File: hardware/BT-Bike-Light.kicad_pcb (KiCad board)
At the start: 4 copper layers, 35 x 80 mm, 40 parts, among them J101 USB_C_Charge_Port, J102 Conn_ARM_SWD_TagConnect_TC203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, J103 BATT, Q101 DMN3731U-7, SW102 Button, U101 BT840, U102 nPM1300, U103 FEM11-F09, U105 TPS92201

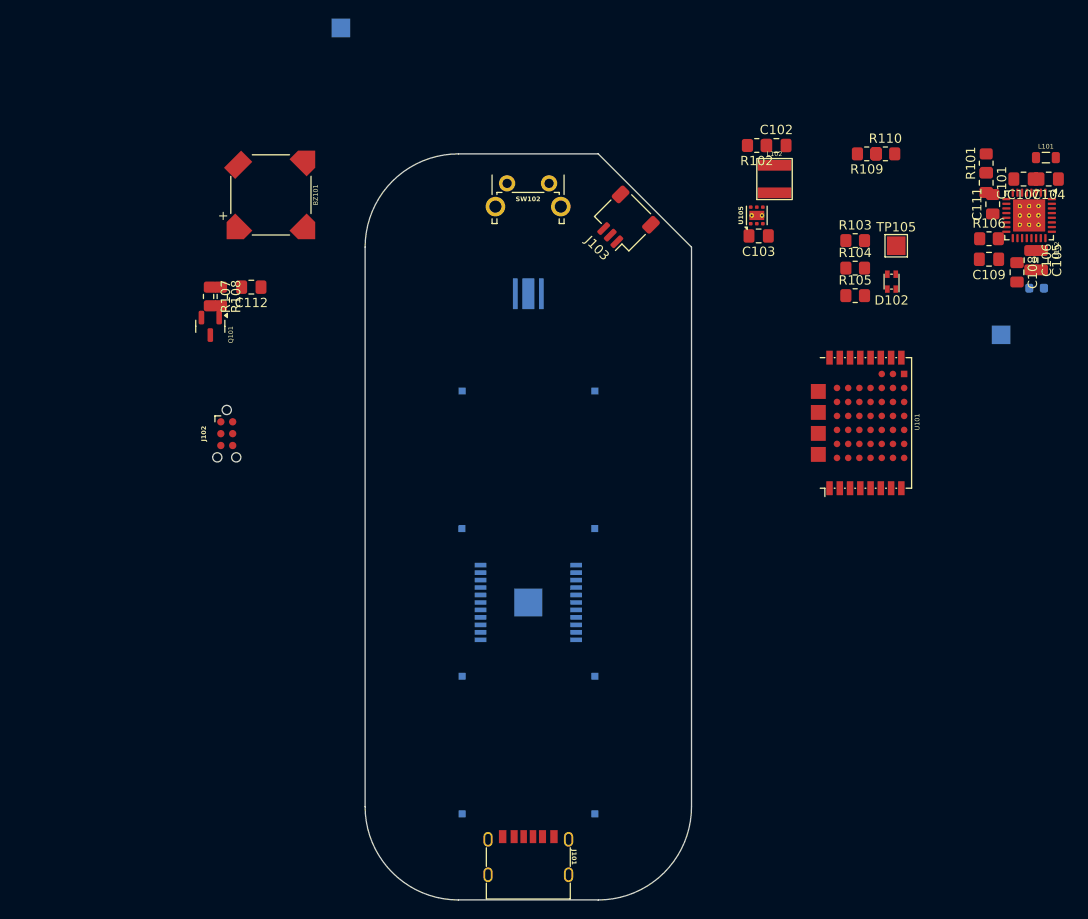
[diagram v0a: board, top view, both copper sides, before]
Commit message: Battery management IC component placement
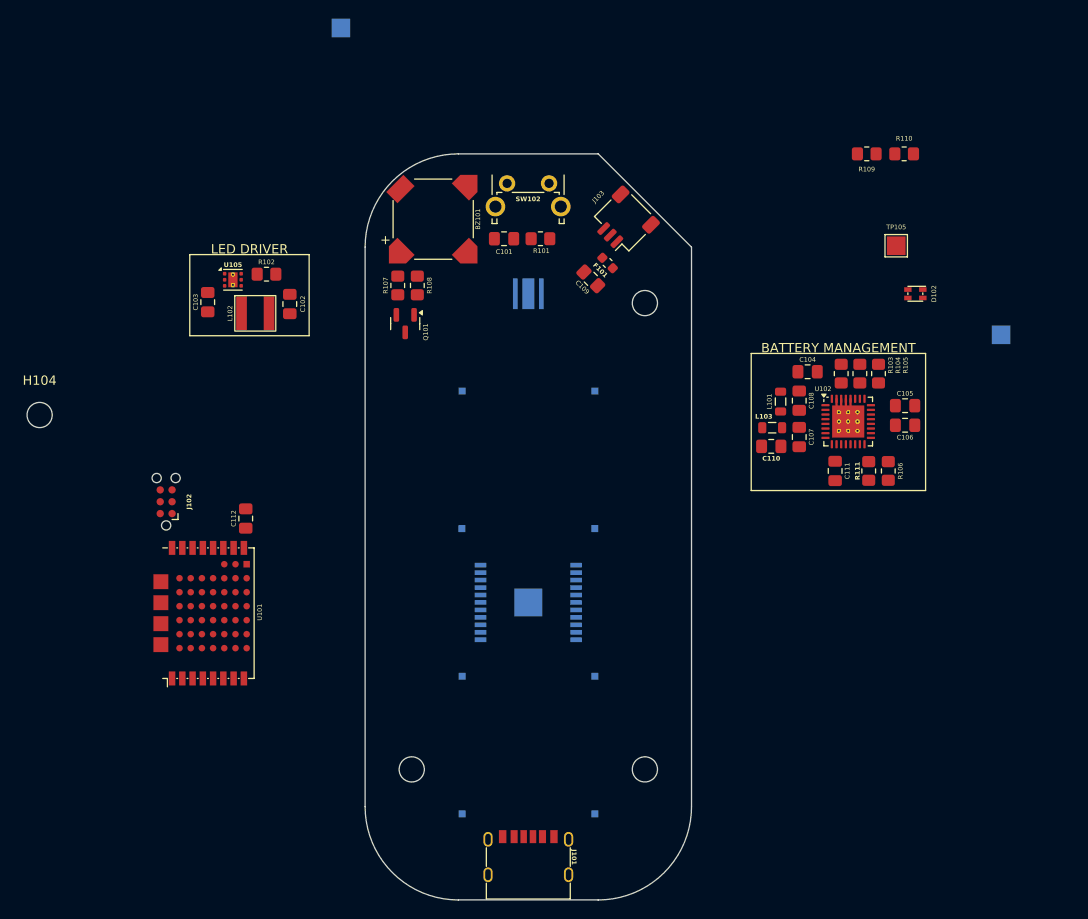
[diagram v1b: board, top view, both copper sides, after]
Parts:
- added C110: 10uF, Capacitor_SMD:C_0805_2012Metric_Pad1.18x1.45mm_HandSolder, F.Cu at (168.6, 96.4)
- added H101: M2.5, MountingHole:MountingHole_2.7mm_M2.5, F.Cu at (130.0, 131.0)
- added H102: M2.5, MountingHole:MountingHole_2.7mm_M2.5, F.Cu at (155.0, 131.0)
- added H103: M2.5, MountingHole:MountingHole_2.7mm_M2.5, F.Cu at (155.0, 81.0)
- added H104: M2.5, MountingHole:MountingHole_2.7mm_M2.5, F.Cu at (90.1, 93.0)
- added L103: 2.2uH, Inductor_SMD:L_0805_2012Metric, F.Cu at (168.7, 94.4)
- added R111: 68k, Resistor_SMD:R_0805_2012Metric_Pad1.20x1.40mm_HandSolder, F.Cu at (179.0, 99.0)
- F101: moved to F.Cu
- moved U101 73.4 mm to (104.3, 121.2)
- moved C103 59.5 mm to (108.1, 80.9), turned to -90 degrees
- moved L102 57.5 mm to (113.2, 82.1), turned to 0 degrees
- moved U105 56.6 mm to (110.8, 78.5), turned to 0 degrees
- moved C102 54.9 mm to (116.9, 81.1), turned to 90 degrees
- moved R102 54.4 mm to (114.4, 77.9)
- moved C101 52.0 mm to (139.9, 74.1), turned to 180 degrees
- moved R101 48.5 mm to (143.8, 74.1), turned to 0 degrees
- moved F101 46.1 mm to (151.0, 76.7), turned to -45 degrees
- moved C109 42.8 mm to (149.2, 78.4), turned to 135 degrees
- moved L101 38.7 mm to (169.6, 91.6), turned to 90 degrees
- moved C107 36.7 mm to (171.6, 95.4), turned to -90 degrees
- moved C111 33.2 mm to (175.4, 99.0), turned to -90 degrees
- moved C104 33.1 mm to (172.4, 88.4), turned to 0 degrees
- moved U102 29.4 mm to (176.8, 93.7), turned to 0 degrees
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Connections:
- U102 pad 16: GND -> Net-(U102-VSET2)
- U102 pad 32: unconnected-(U102-VOUT2-Pad32) -> +2V6
- U102 pad 5: unconnected-(U102-SW2-Pad5) -> Net-(U102-SW2)
- U102 pad 6: unconnected-(U102-PVSS2-Pad6) -> GND
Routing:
- net GND: track 0.00 -> 6.16 mm
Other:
- board text added: "BATTERY MANAGEMENT"
- board text added: "LED DRIVER"
- board text removed: "+"
- board text removed: "-"

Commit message: Component placement
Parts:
- removed H104: M2.5, MountingHole:MountingHole_2.7mm_M2.5
- TP105: value 1V8 -> 2V6; moved to B.Cu
- moved D102 69.8 mm to (149.1, 140.4), turned to 0 degrees
- moved TP103 65.7 mm to (127.7, 80.0), turned to 180 degrees
- moved TP105 63.4 mm to (130.2, 111.5), turned to 180 degrees
- moved R110 59.1 mm to (142.2, 107.9), turned to -90 degrees
- moved R109 57.7 mm to (140.2, 107.9), turned to -90 degrees
- moved BZ101 46.0 mm to (131.0, 118.0), turned to 180 degrees
- moved TP104 41.3 mm to (143.5, 87.0), turned to 0 degrees
- moved C105 35.1 mm to (149.0, 83.0), turned to 180 degrees
- moved U101 33.4 mm to (132.9, 104.1)
- moved R105 33.3 mm to (147.0, 85.1), turned to 0 degrees
- moved C106 33.1 mm to (152.1, 82.2), turned to 90 degrees
- moved C112 32.4 mm to (140.1, 87.5), turned to 180 degrees
- moved R108 32.4 mm to (132.0, 111.5), turned to 180 degrees
- moved J102 31.5 mm to (131.0, 86.7), turned to 0 degrees
- moved R104 31.1 mm to (147.0, 87.1), turned to 0 degrees
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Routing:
- net VSYS: track 0.00 -> 17.7 mm, vias 0 -> 2
- net GND: track 6.16 -> 19.7 mm
- net +2V6: track 0.00 -> 12.6 mm, vias 0 -> 2
- net +1V8: track 0.00 -> 5.84 mm
- net Net-(U102-SW1): track 0.00 -> 5.72 mm
- net Net-(U102-SW2): track 0.00 -> 5.46 mm
- net Net-(U102-VSET1): track 0.00 -> 3.41 mm
- net VBUSOUT: track 0.00 -> 3.41 mm
- net Net-(U105-SW): track 0.00 -> 2.97 mm
- net VBUS: track 0.00 -> 2.81 mm
- net /LED_R: track 0.00 -> 2.50 mm
- net /LED_B: track 0.00 -> 2.50 mm
- net Net-(D101-A): track 0.00 -> 2.24 mm
- net Net-(U102-VSET2): track 0.00 -> 2.05 mm
- net Net-(D101-K): track 0.00 -> 1.73 mm
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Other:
- board text added: "BLUETOOTH"
- board text added: "BUZZER"
- board text added: "POWER MGMT"
- board text removed: "BATTERY MANAGEMENT"

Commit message: Schematic cleanup
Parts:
- moved BZ101 5.00 mm to (131.0, 113.0)
- moved C101 5.00 mm to (139.9, 69.1)
- moved C102 5.00 mm to (133.7, 66.1)
- moved C103 5.00 mm to (133.5, 74.9)
- moved C104 5.00 mm to (146.8, 87.7)
- moved C105 5.00 mm to (149.0, 78.0)
- moved C106 5.00 mm to (152.1, 77.2)
- moved C107 5.00 mm to (153.8, 88.6)
- moved C108 5.00 mm to (149.9, 88.6)
- moved C109 5.00 mm to (157.2, 70.6)
- moved C110 5.00 mm to (154.8, 91.6)
- moved C111 5.00 mm to (157.4, 84.8)
- moved C112 5.00 mm to (140.1, 82.5)
- moved D101 5.00 mm to (142.5, 75.0)
- moved D102 5.00 mm to (149.1, 135.4)
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
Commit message: Route board
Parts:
- removed R103, R104, R105: 110, Resistor_SMD:R_0805_2012Metric_Pad1.20x1.40mm_HandSolder
- added TP101: VBUS, TestPoint:TestPoint_Pad_2.0x2.0mm, B.Cu at (155.3, 133.2)
- J102: value Conn_ARM_SWD_TagConnect_TC2030-NL -> TagConnect; moved to B.Cu
- moved R109 0.30 mm to (139.9, 102.9)
- moved R110 0.30 mm to (141.9, 102.9)
- moved C101 0.15 mm to (139.8, 69.1)
- moved R101 0.15 mm to (143.7, 69.1)
- turned D102 to 180 degrees
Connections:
- D102 pad 1: Net-(D102-GK) -> /LED_G
- D102 pad 2: Net-(D102-BK) -> /LED_B
- D102 pad 4: Net-(D102-RK) -> /LED_R
- U101 pad 1: unconnected-(U101-P0.26-Pad1) -> /BUZZER
- U101 pad 11: /BUZZER -> /BTN
- U101 pad 12: unconnected-(U101-P1.00-Pad12) -> /LED_EN
- U101 pad 13: unconnected-(U101-P0.13-Pad13) -> /LED_PWM
- U101 pad 2: /LED_EN -> unconnected-(U101-P0.27-Pad2)
- U101 pad 3: /LED_PWM -> unconnected-(U101-P0.00-Pad3)
- U101 pad 6: /BTN -> unconnected-(U101-P0.03-Pad6)
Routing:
- net VSYS: track 17.7 -> 156.6 mm, vias 2 -> 4
- net VBUS: track 2.81 -> 84.4 mm, vias 0 -> 2
- net +1V8: track 5.84 -> 79.4 mm, vias 0 -> 3
- net Net-(J101-CC1): track 0.00 -> 58.7 mm
- net GND: track 19.7 -> 78.3 mm, vias 0 -> 140
- net /LED_R: track 2.50 -> 59.4 mm
- net Net-(J101-CC2): track 0.00 -> 56.5 mm
- net /LED_G: track 1.70 -> 56.9 mm
- net /LED_B: track 2.50 -> 56.3 mm
- net /BTN: track 0.00 -> 48.3 mm, vias 0 -> 2
- net +2V6: track 12.6 -> 60.4 mm, vias 2 -> 1
- net /SDA: track 0.00 -> 33.4 mm, vias 0 -> 2
- net /SCL: track 0.00 -> 33.1 mm, vias 0 -> 3
- net Net-(D101-K): track 1.73 -> 18.4 mm, vias 0 -> 1
- net /BATT_NTC: track 0.00 -> 16.1 mm, vias 0 -> 2
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- added copper zone on B.Cu, net GND
- added copper zone on F.Cu, net GND
- added copper zone on In1.Cu, net GND
- added copper zone on In2.Cu, net GND

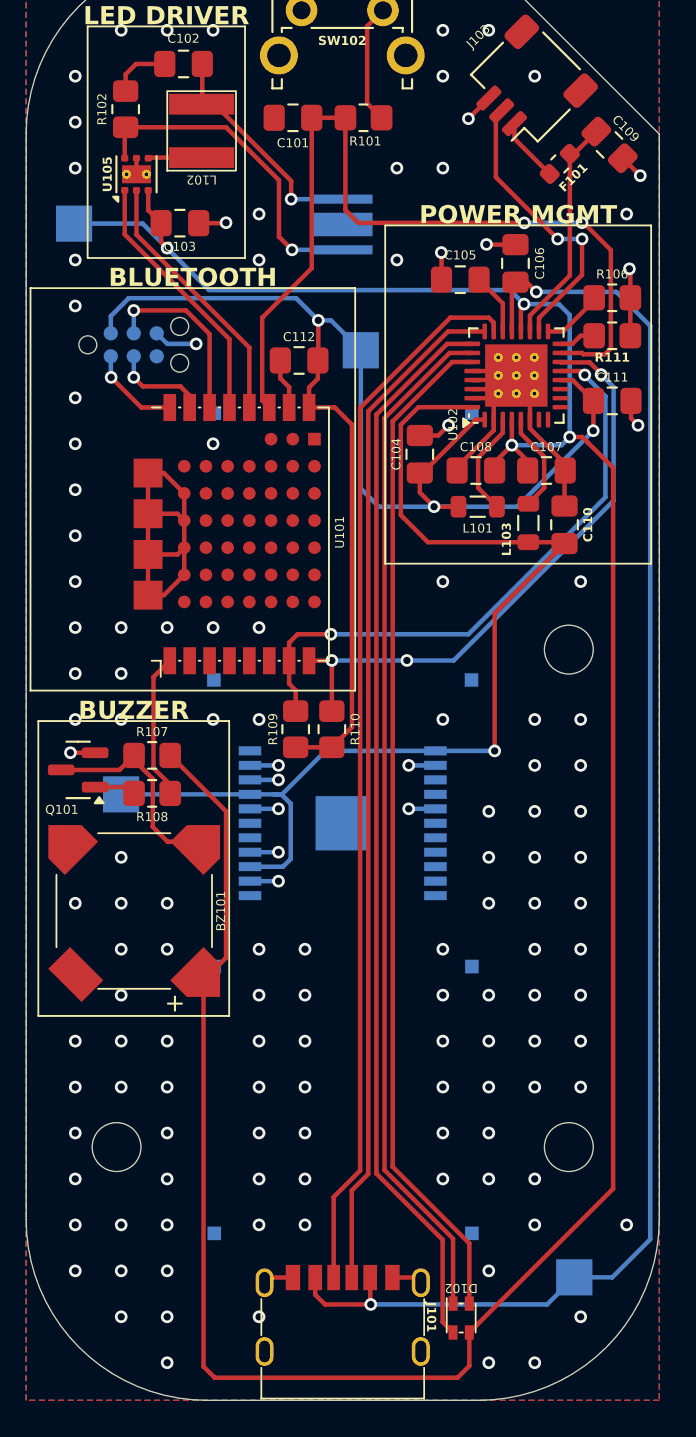
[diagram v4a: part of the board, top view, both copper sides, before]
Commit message: Combine 1V8 and 2V6 line to 2V6
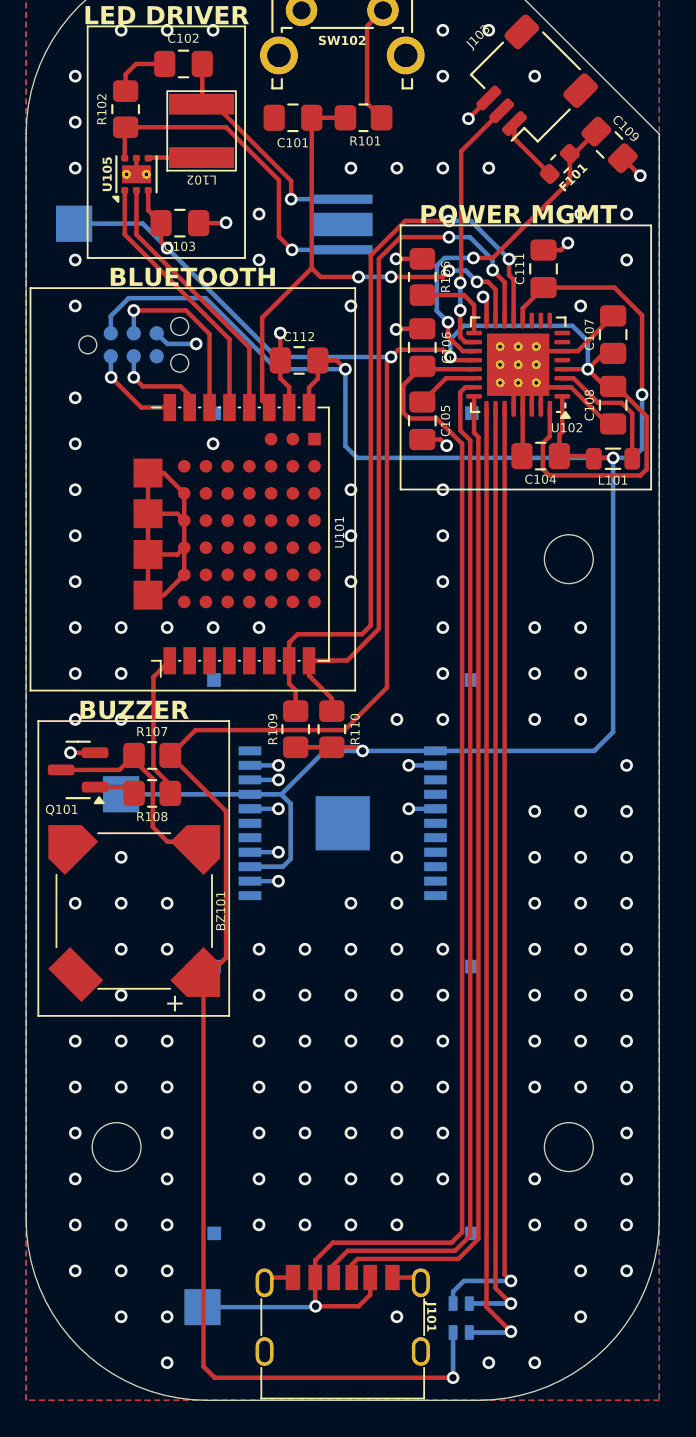
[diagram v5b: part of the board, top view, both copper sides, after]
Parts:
- removed C110: 10uF, Capacitor_SMD:C_0805_2012Metric_Pad1.18x1.45mm_HandSolder
- removed L103: 2.2uH, Inductor_SMD:L_0805_2012Metric
- removed R111: 68k, Resistor_SMD:R_0805_2012Metric_Pad1.20x1.40mm_HandSolder
- removed TP104: 1V8, TestPoint:TestPoint_Pad_2.0x2.0mm
- D102: moved to B.Cu
- R106: value 47k -> 68k
- moved TP101 20.6 mm to (134.8, 134.8)
- moved R106 10.6 mm to (146.9, 77.9), turned to -90 degrees
- moved C108 8.40 mm to (157.4, 85.0), turned to -90 degrees
- moved C107 8.37 mm to (157.4, 81.1), turned to 90 degrees
- moved C111 8.23 mm to (153.6, 77.5), turned to 90 degrees
- moved C105 8.08 mm to (146.9, 85.8), turned to -90 degrees
- moved L101 7.94 mm to (157.4, 88.0)
- moved C106 6.94 mm to (146.9, 81.8)
- moved C104 6.68 mm to (153.4, 87.8), turned to 180 degrees
- moved H103 5.00 mm to (155.0, 93.5)
- moved U102 0.61 mm to (152.2, 82.8), turned to 180 degrees
- turned D102 to 0 degrees
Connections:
- C104 pad 1: +1V8 -> +2V6
- C111 pad 1: +1V8 -> +2V6
- C112 pad 1: +1V8 -> +2V6
- J102 pad 1: +1V8 -> +2V6
- L101 pad 2: +1V8 -> +2V6
- R109 pad 2: +1V8 -> +2V6
- R110 pad 2: +1V8 -> +2V6
- U101 pad 9: +1V8 -> +2V6
- U102 pad 1: +1V8 -> +2V6
- U102 pad 12: +1V8 -> +2V6
- U102 pad 16: Net-(U102-VSET2) -> GND
- U102 pad 32: +2V6 -> VSYS
- U102 pad 5: Net-(U102-SW2) -> unconnected-(U102-SW2-Pad5)
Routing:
- net +1V8: track 79.4 -> 0.00 mm, vias 3 -> 0
- net +2V6: track 60.4 -> 117.6 mm, vias 1 -> 4
- net /BTN: track 48.3 -> 31.8 mm, vias 2 -> 4
- net VSYS: track 156.6 -> 144.0 mm, vias 4 -> 5
- net VBUS: track 84.4 -> 75.3 mm, vias 2 -> 1
- net /SDA: track 33.4 -> 42.1 mm
- net /SCL: track 33.1 -> 39.3 mm, vias 3 -> 2
- net +BATT: track 12.7 -> 18.7 mm, vias 0 -> 2
- net Net-(U102-SW2): track 5.55 -> 0.00 mm
- net /LED_R: track 59.4 -> 53.9 mm, vias 0 -> 1
- net /LED_G: track 56.9 -> 52.1 mm, vias 0 -> 1
- net /LED_B: track 56.3 -> 52.5 mm, vias 0 -> 1
- net Net-(J101-CC1): track 58.7 -> 56.6 mm
- net Net-(U102-VSET2): track 2.05 -> 0.00 mm
- net /BATT_NTC: track 16.1 -> 14.3 mm
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
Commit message: Schematic cleanup and add test points
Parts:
- removed TP103: VSYS, TestPoint:TestPoint_Pad_2.0x2.0mm
- removed TP105: 2V6, TestPoint:TestPoint_Pad_2.0x2.0mm
- added TP102: VBUS, TestPoint:TestPoint_Pad_2.0x2.0mm, B.Cu at (134.8, 134.8)
- added TP104: VSYS, TestPoint:TestPoint_Pad_2.0x2.0mm, B.Cu at (127.6, 75.0)
- added TP106: 2V6, TestPoint:TestPoint_Pad_2.0x2.0mm, B.Cu at (157.2, 77.1)
- TP101: value VBUS -> GND
- moved TP101 70.7 mm to (134.2, 64.2)
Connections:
- D101 pad 3: unconnected-(D101-PAD-Pad3) -> GND
- TP101 pad 1: VBUS -> GND
- U101 pad 4: /ACCEL_INT2 -> unconnected-(U101-P0.01-Pad4)
- U101 pad 5: /ACCEL_INT1 -> unconnected-(U101-P0.02-Pad5)
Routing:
- net GND: track 77.6 -> 73.3 mm, vias 174 -> 171
- net +2V6: track 117.6 -> 118.5 mm
- net VSYS: track 144.0 -> 144.6 mm

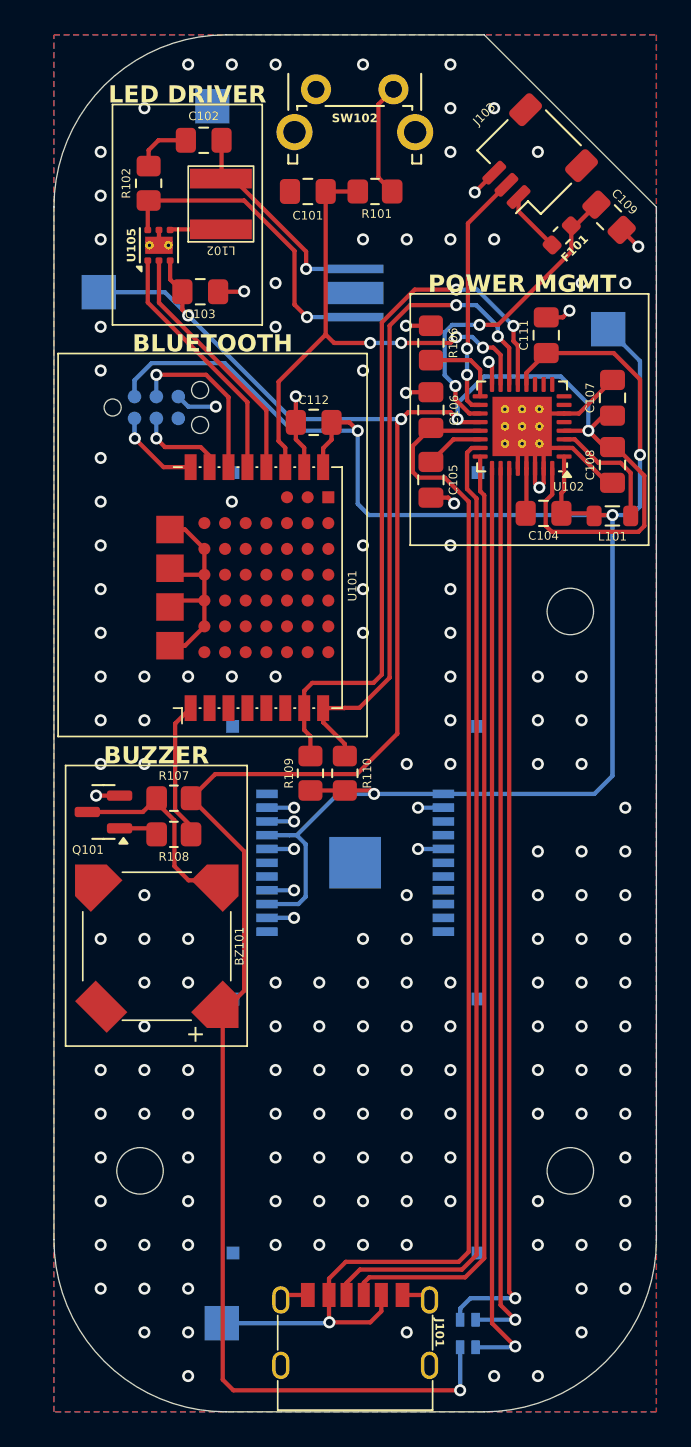
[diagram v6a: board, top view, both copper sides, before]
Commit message: Schematic and PCB cleanup
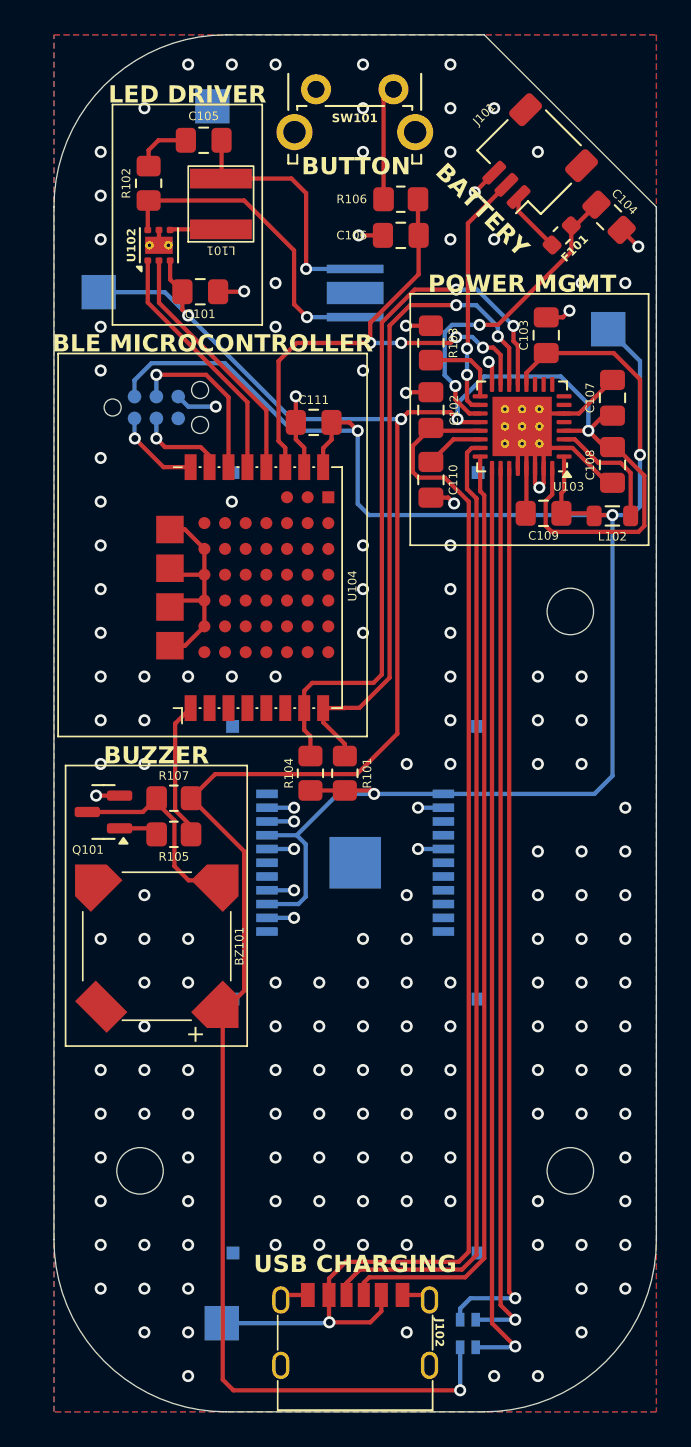
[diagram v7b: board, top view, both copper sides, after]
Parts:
- moved G*** 65.4 mm to (142.5, 135.2)
- moved C106 5.97 mm to (145.2, 71.7)
- moved R106 1.57 mm to (145.2, 69.5), turned to 180 degrees
- renumbered C103 to C101, C106 to C102, C111 to C103, C109 to C104, C102 to C105, C101 to C106, C104 to C109, C105 to C110, C112 to C111, D102 to D101, D101 to D102, J103 to J101, J101 to J102, J102 to J103, L102 to L101, L101 to L102, R110 to R101, R106 to R103, R109 to R104, R108 to R105, R101 to R106, SW102 to SW101, U103 to U101, U105 to U102, U102 to U103, U101 to U104
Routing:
- net Net-(D102-A): track 12.8 -> 14.8 mm
- net GND: track 73.3 -> 74.7 mm, vias 171 -> 172
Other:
- board text added: "BATTERY"
- board text added: "BLE MICROCONTROLLER"
- board text added: "BUTTON"
- board text added: "DEBUG HEADER"
- board text added: "LED"
- board text added: "RADAR MODULE"
- board text added: "USB CHARGING"
- board text removed: "BLUETOOTH"
